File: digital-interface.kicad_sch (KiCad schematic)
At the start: 37 parts, among them U301 Si8641BD-B-IS2, U302 R05C05TE05S

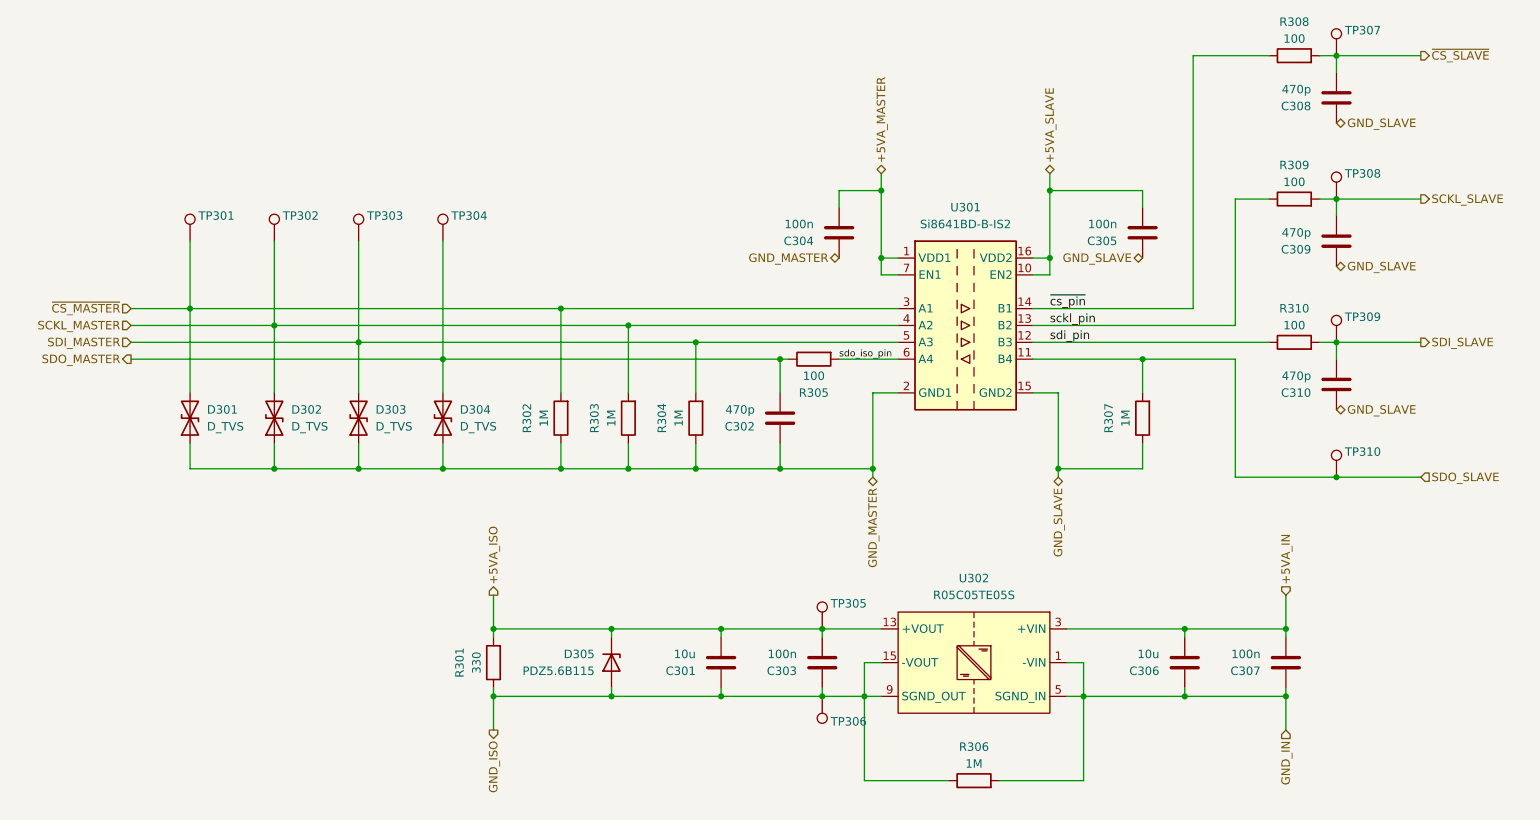
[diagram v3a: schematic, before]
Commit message: separate digital-interface and iso-dcdc
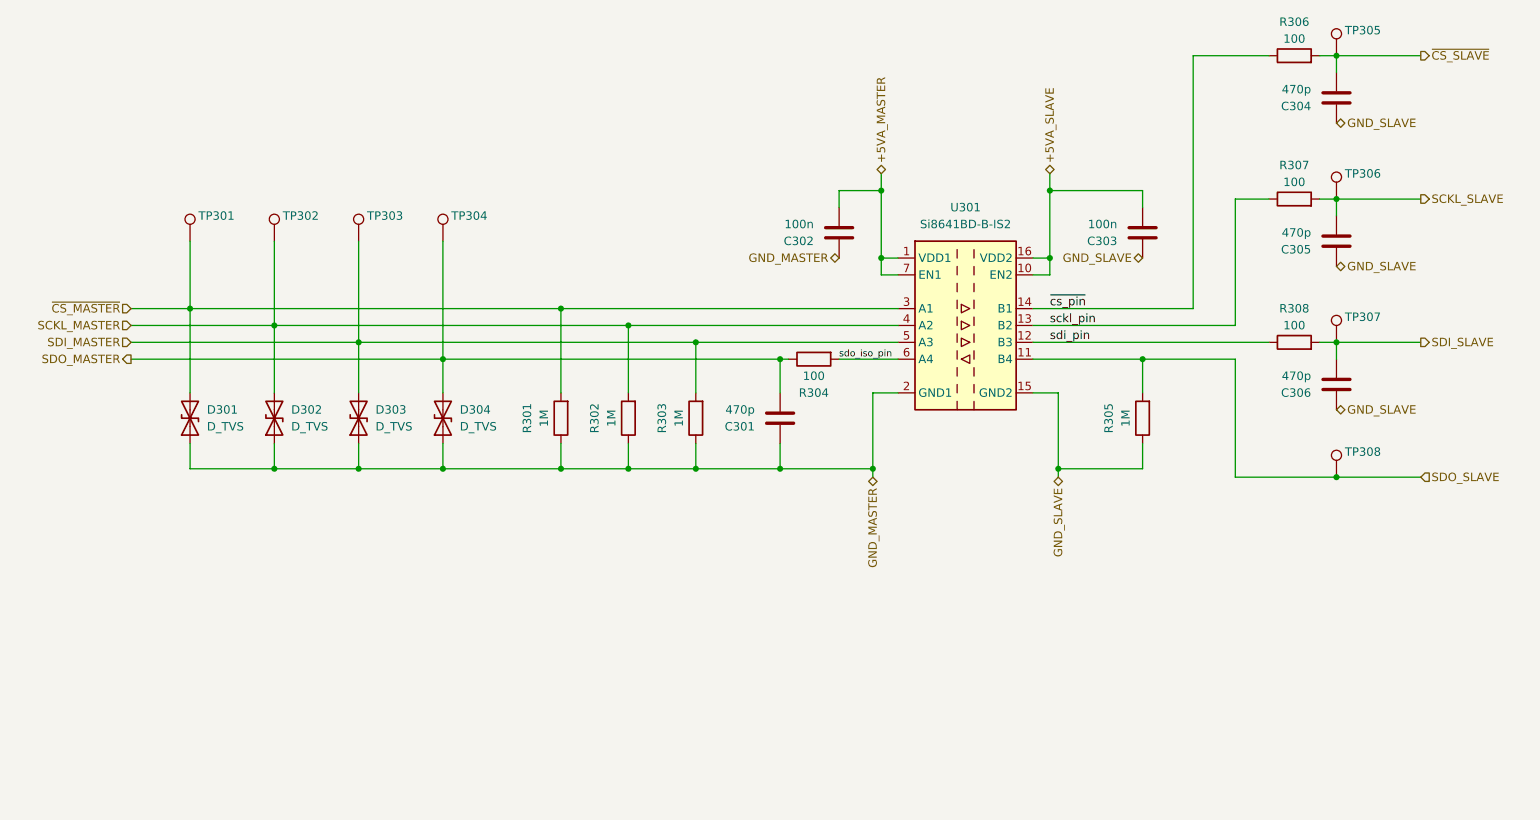
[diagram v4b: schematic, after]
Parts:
- removed C301, C306: 10u, meas:C_1210_3225Metric_Pad1.33x2.70mm_HandSolder, symbol meas:C
- removed C303, C307: 100n, meas:C_0805_2012Metric_Pad1.18x1.45mm_HandSolder, symbol meas:C
- removed D305: PDZ5.6B115, meas:D_SOD-323_HandSoldering, symbol meas:D_Zener
- removed R301: 330, meas:R_1210_3225Metric_Pad1.30x2.65mm_HandSolder, symbol meas:R
- removed R306: 1M, meas:R_1210_3225Metric_Pad1.30x2.65mm_HandSolder, symbol meas:R
- removed TP305, TP306: ~, meas:TP_0805_2012Metric, symbol meas:TestPoint
- removed U302: R05C05TE05S, meas:SOIC-16W_7.5x10.3mm_P1.27mm, symbol meas:R05C05TE05S
- renumbered C302 to C301, C304 to C302, C305 to C303, C308 to C304, C309 to C305, C310 to C306, R302 to R301, R303 to R302, R304 to R303, R305 to R304, R307 to R305, R308 to R306, R309 to R307, R310 to R308, TP307 to TP305, TP308 to TP306, TP309 to TP307, TP310 to TP308

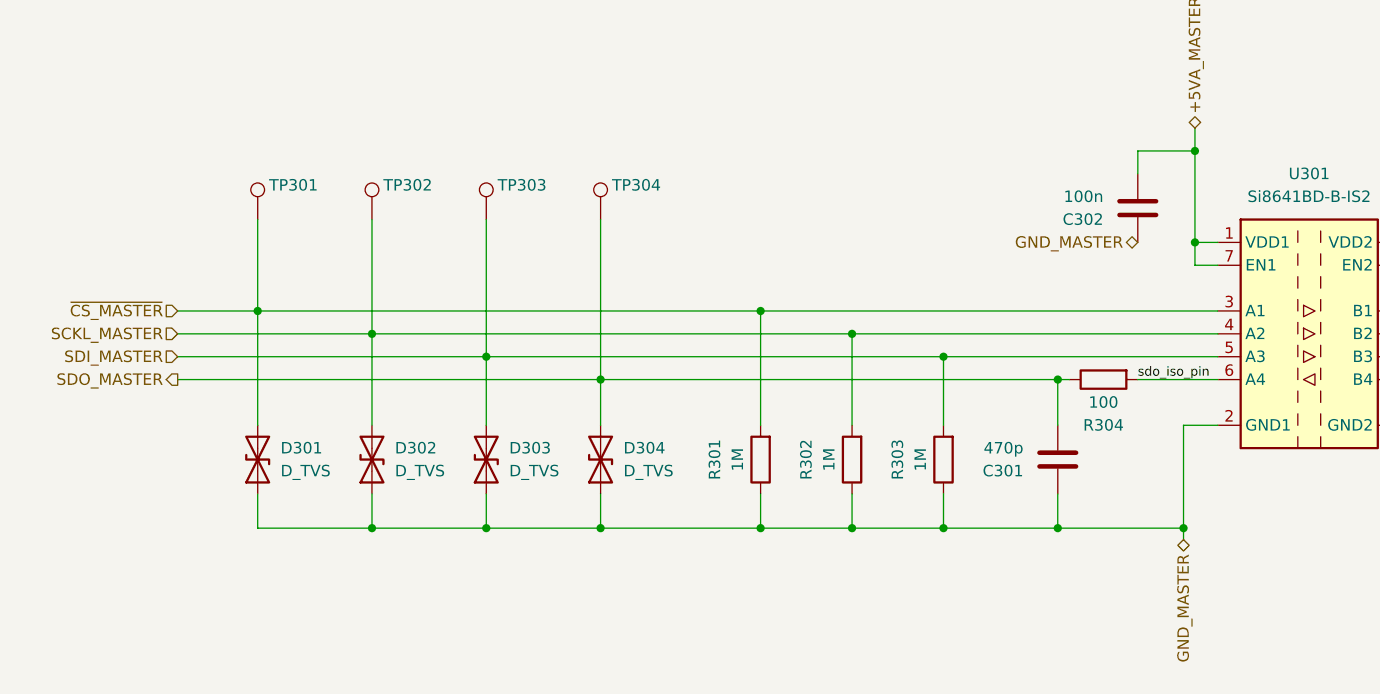
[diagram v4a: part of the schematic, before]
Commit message: fix filled zone netnumbers
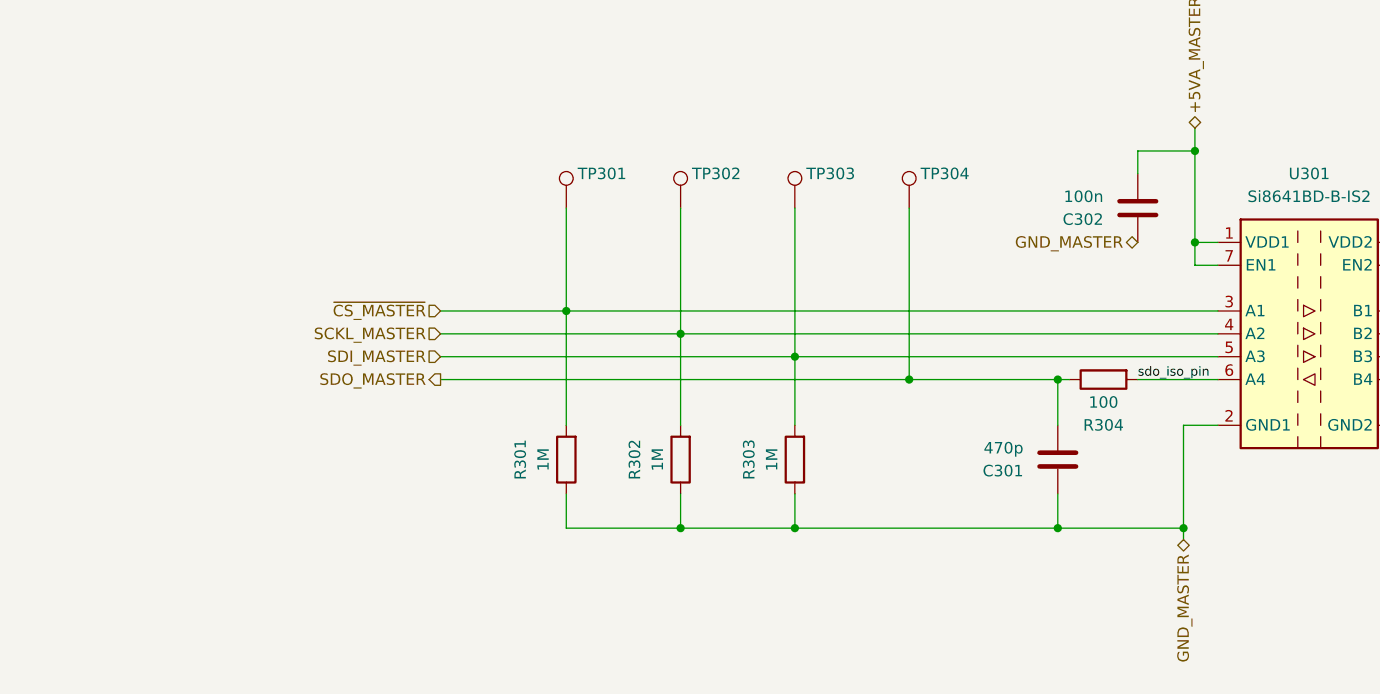
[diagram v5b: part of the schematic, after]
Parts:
- removed D301, D302, D303, D304: D_TVS, meas:D_SOD-323_HandSoldering, symbol meas:D_TVS
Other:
- moved on the sheet: R301, R302, R303, TP301, TP302, TP303, TP304
